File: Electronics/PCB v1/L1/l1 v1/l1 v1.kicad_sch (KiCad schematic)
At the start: 168 parts, among them J1 Conn_01x01_Socket, J2 Conn_01x01_Socket, SW1 SW_SPDT, U1 ESP32-S3-DEVKITM-1-N8

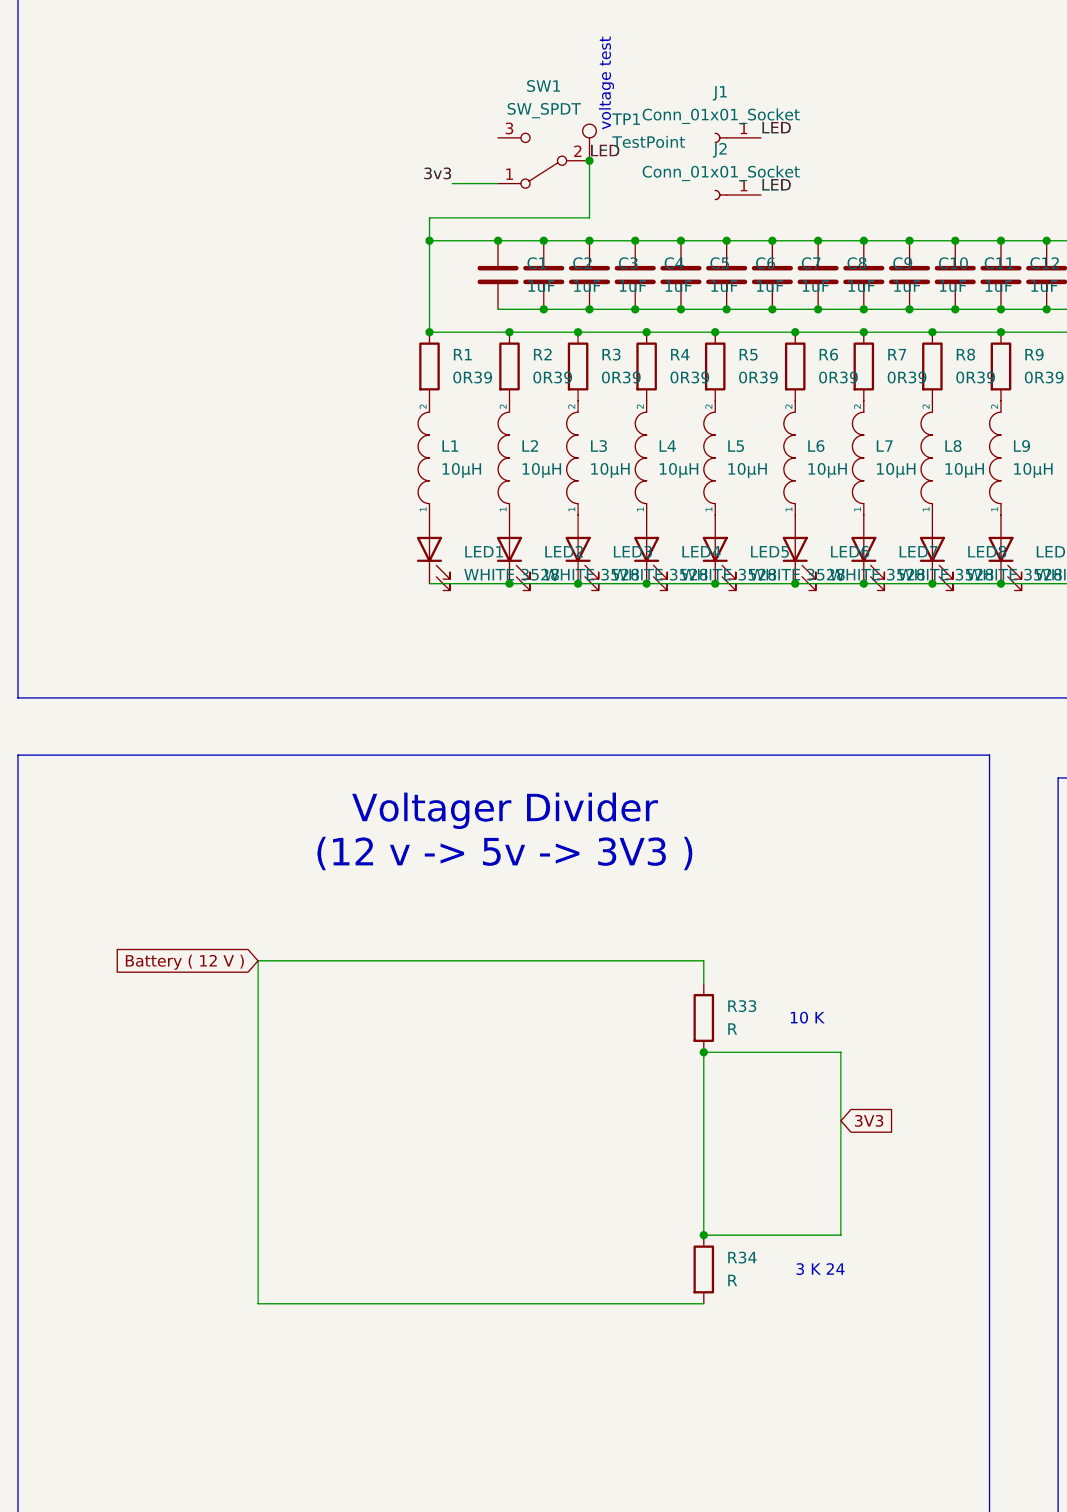
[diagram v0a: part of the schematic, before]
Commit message: updated ver of L1 with buck converter 21 11 2024
new ver xcbhc
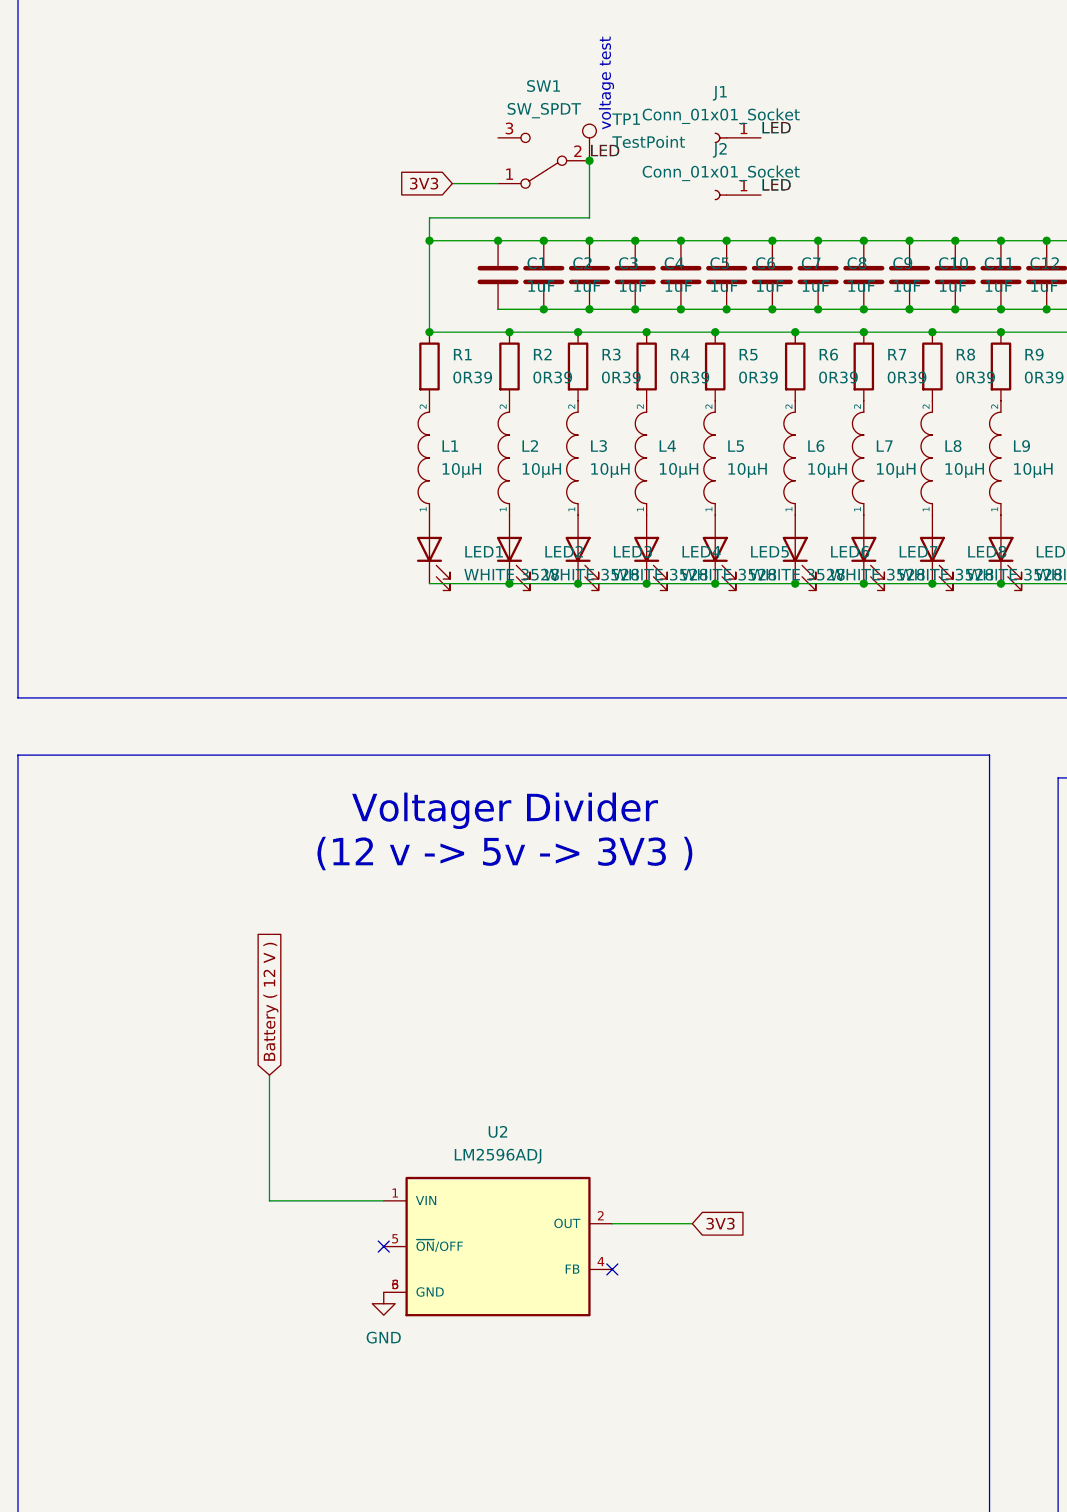
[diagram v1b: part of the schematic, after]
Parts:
- removed R33, R34: R, symbol Device:R
- added U2: LM2596ADJ, LM2596ADJ:LM2596ADJ, symbol LM2596AD:LM2596ADJ
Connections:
- net 3v3 is gone; now on net 3V3: SW1.1 (A)
- net 3V3: now also U2.2 (OUT)
- net Battery ( 12 V ): now also U2.1 (VIN)
- net GND: now also U2.3 (GND), U2.6 (GND)
- no-connect marks 8 -> 10
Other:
- note removed: "10 K"
- note removed: "3 K 24"
